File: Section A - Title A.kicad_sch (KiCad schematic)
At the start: 9 parts, among them J2 THD-02-R, J3 Conn_01x22_Female, J4 690-019-298-412, U2 RT9742SNGV

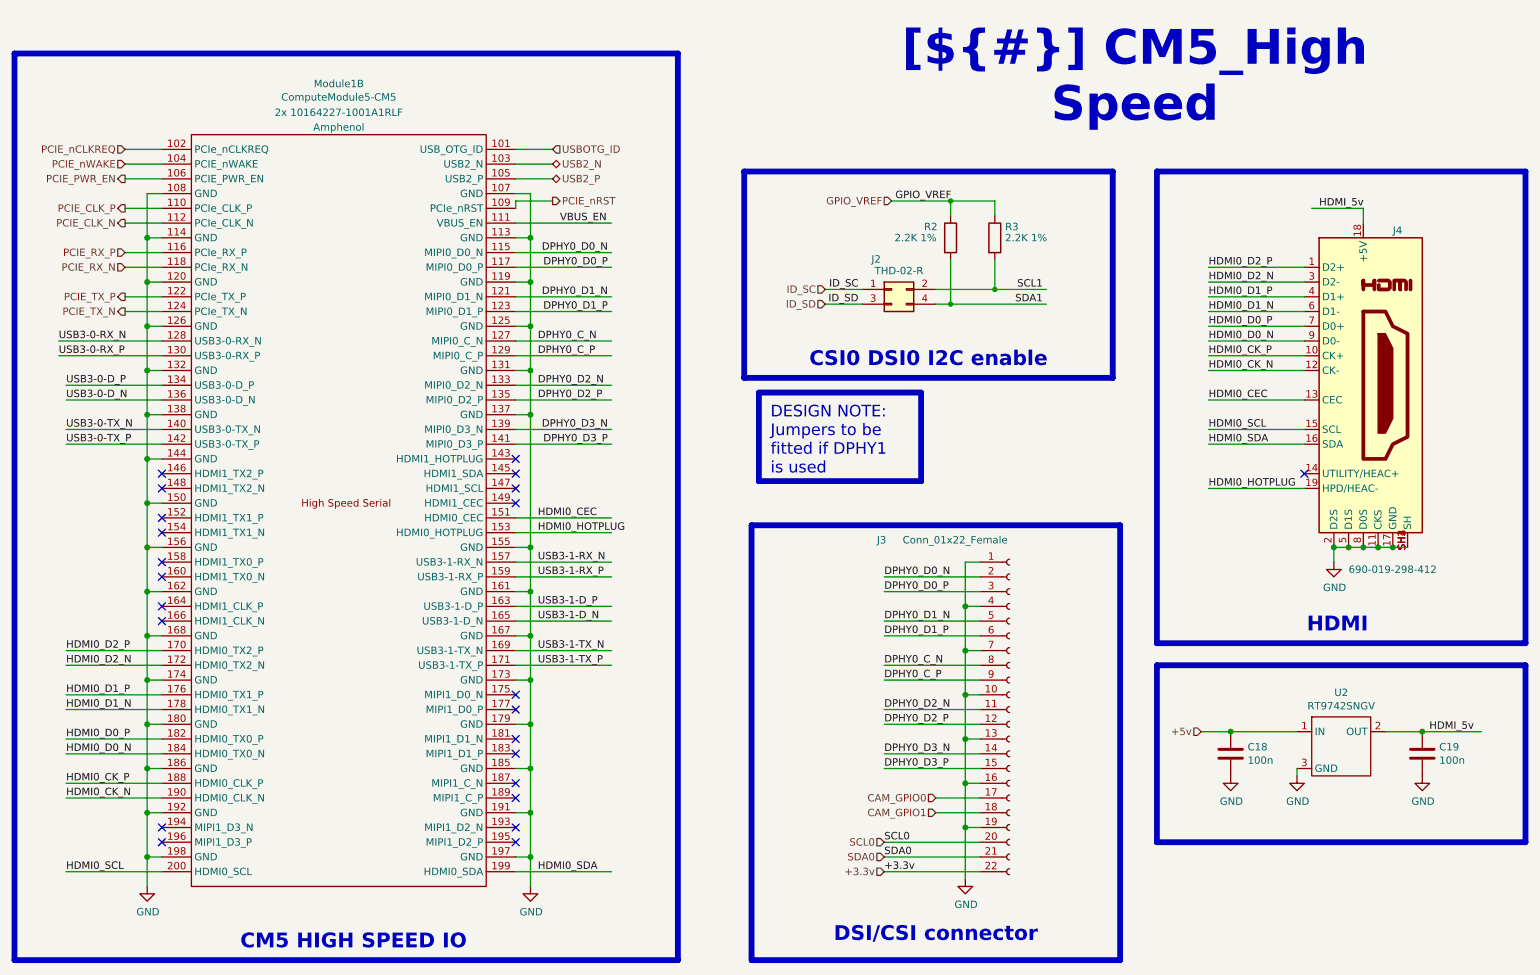
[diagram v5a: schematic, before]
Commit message: Swiitched to JSM561
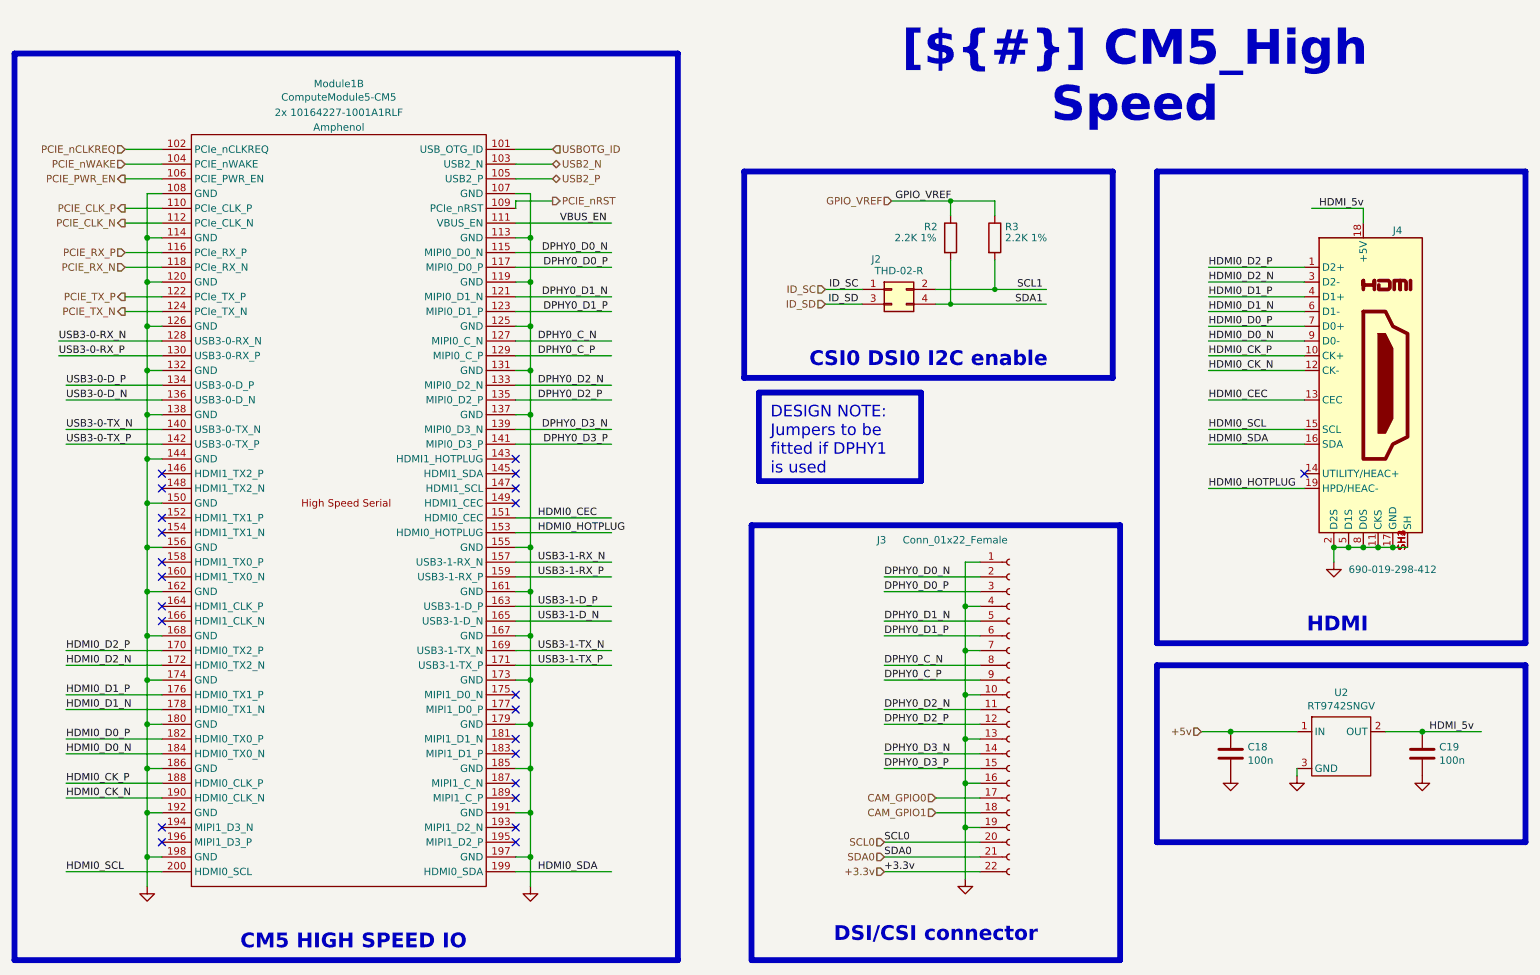
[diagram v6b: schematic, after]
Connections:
- removed net GND: C18.2, C19.2, J3.1 (Pin_1), J3.10 (Pin_10), J3.13 (Pin_13), J3.16 (Pin_16), J3.19 (Pin_19), J3.4 (Pin_4), J3.7 (Pin_7), J4.11 (CKS), J4.17 (GND), J4.2 (D2S), J4.5 (D1S), J4.8 (D0S), J4.SH1 (SH), J4.SH2 (SH), J4.SH3 (SH), J4.SH4 (SH), Module1.107 (GND), Module1.108 (GND), Module1.113 (GND), Module1.114 (GND), Module1.119 (GND), Module1.120 (GND), Module1.125 (GND), Module1.126 (GND), Module1.131 (GND), Module1.132 (GND), Module1.137 (GND), Module1.138 (GND), Module1.144 (GND), Module1.150 (GND), Module1.155 (GND), Module1.156 (GND), Module1.161 (GND), Module1.162 (GND), Module1.167 (GND), Module1.168 (GND), Module1.173 (GND), Module1.174 (GND), Module1.179 (GND), Module1.180 (GND), Module1.185 (GND), Module1.186 (GND), Module1.191 (GND), Module1.192 (GND), Module1.197 (GND), Module1.198 (GND), U2.3 (GND)
- new net: J3.1 (Pin_1), J3.10 (Pin_10), J3.13 (Pin_13), J3.16 (Pin_16), J3.19 (Pin_19), J3.4 (Pin_4), J3.7 (Pin_7)
- new net: J4.11 (CKS), J4.17 (GND), J4.2 (D2S), J4.5 (D1S), J4.8 (D0S), J4.SH1 (SH), J4.SH2 (SH), J4.SH3 (SH), J4.SH4 (SH)
- new net: Module1.107 (GND), Module1.113 (GND), Module1.119 (GND), Module1.125 (GND), Module1.131 (GND), Module1.137 (GND), Module1.155 (GND), Module1.161 (GND), Module1.167 (GND), Module1.173 (GND), Module1.179 (GND), Module1.185 (GND), Module1.191 (GND), Module1.197 (GND)
- new net: Module1.108 (GND), Module1.114 (GND), Module1.120 (GND), Module1.126 (GND), Module1.132 (GND), Module1.138 (GND), Module1.144 (GND), Module1.150 (GND), Module1.156 (GND), Module1.162 (GND), Module1.168 (GND), Module1.174 (GND), Module1.180 (GND), Module1.186 (GND), Module1.192 (GND), Module1.198 (GND)
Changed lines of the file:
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@@
 			)
 		)
-		(property "Value" "GND"
+		(property "Value" "~"
 			(at 242.697 108.5342 0)
 			(effects
@@
 			)
 		)
-		(property "Value" "GND"
+		(property "Value" "~"
 			(at 104.267 164.4142 0)
 			(effects
@@
 			)
 		)
-		(property "Value" "GND"
+		(property "Value" "~"
 			(at 38.227 164.4142 0)
 			(effects
@@
 			)
 		)
-		(property "Value" "GND"
+		(property "Value" "~"
 			(at 179.197 163.1442 0)
 			(effects
@@
 			)
 		)
-		(property "Value" "GND"
+		(property "Value" "~"
 			(at 257.937 145.3642 0)
 			(effects
@@
 			)
 		)
-		(property "Value" "GND"
+		(property "Value" "~"
 			(at 224.917 145.3642 0)
 			(effects
@@
 			)
 		)
-		(property "Value" "GND"
+		(property "Value" "~"
 			(at 236.347 145.3642 0)
 			(effects

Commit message: Removed Ethernet
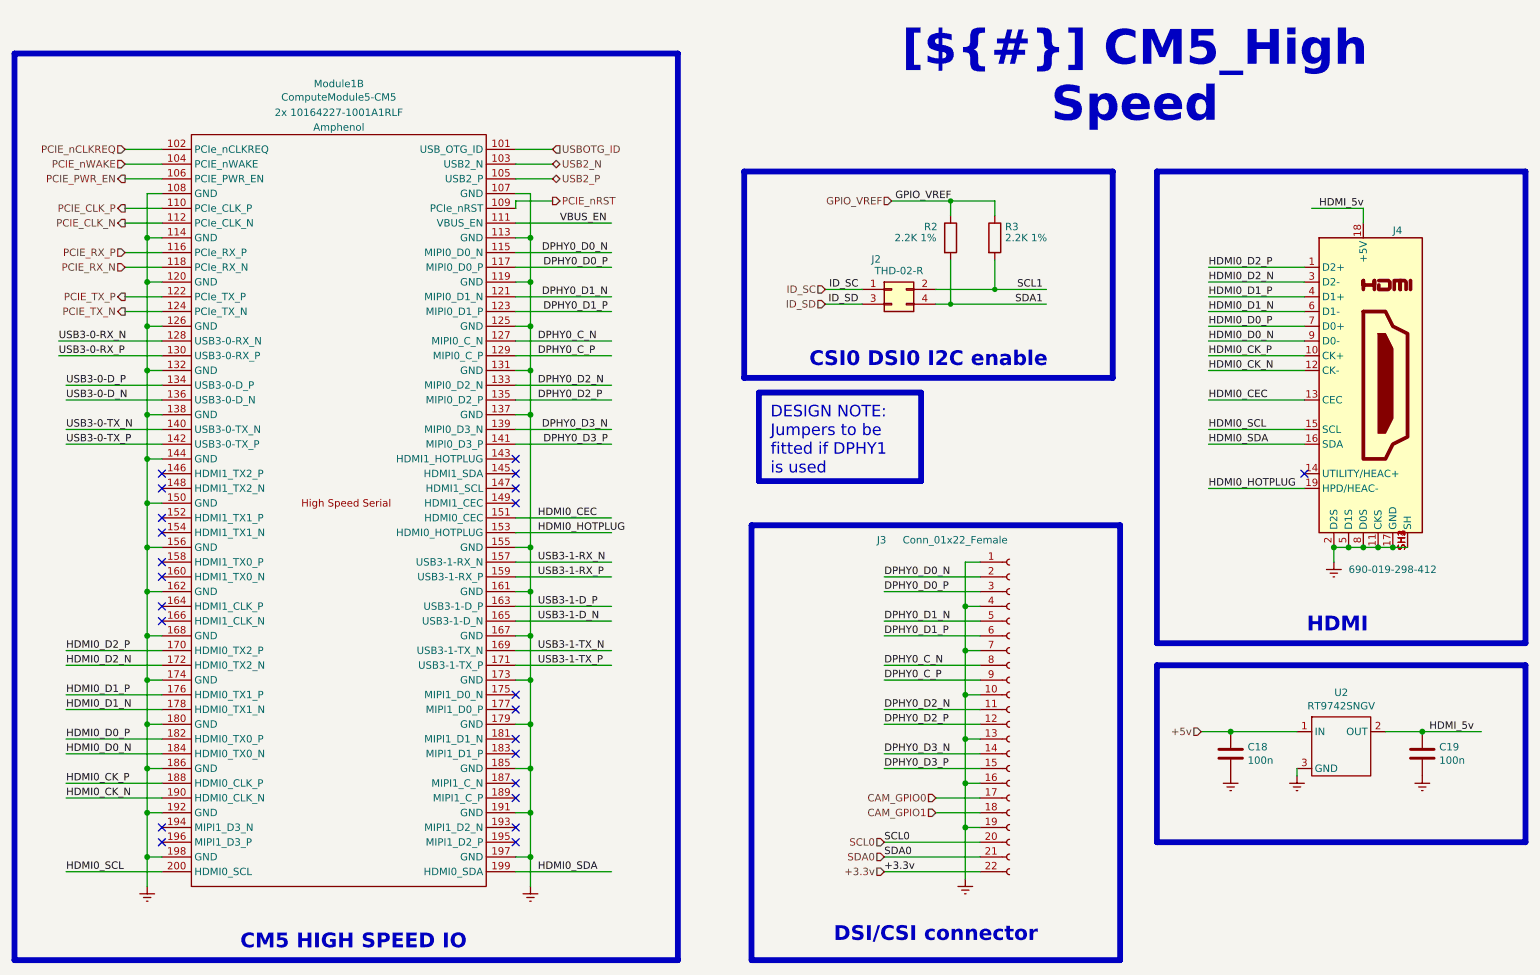
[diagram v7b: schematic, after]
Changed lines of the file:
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@@
 	)
 	(symbol
-		(lib_id "power:GND")
+		(lib_id "power:Earth")
 		(at 242.57 104.14 0)
 		(unit 1)
@@
 			)
 		)
-		(property "Datasheet" ""
+		(property "Datasheet" "~"
 			(at 242.57 104.14 0)
 			(effects
@@
 			)
 		)
-		(property "Description" "Power symbol creates a global label with name \"GND\" , ground"
+		(property "Description" "Power symbol creates a global label with name \"Earth\""
 			(at 242.57 104.14 0)
 			(effects
@@
 	)
 	(symbol
-		(lib_id "power:GND")
+		(lib_id "power:Earth")
 		(at 104.14 160.02 0)
 		(unit 1)
@@
 			)
 		)
-		(property "Datasheet" ""
+		(property "Datasheet" "~"
 			(at 104.14 160.02 0)
 			(effects
@@
 			)
 		)
-		(property "Description" "Power symbol creates a global label with name \"GND\" , ground"
+		(property "Description" "Power symbol creates a global label with name \"Earth\""
 			(at 104.14 160.02 0)
 			(effects
@@
 	)
 	(symbol
-		(lib_id "power:GND")
+		(lib_id "power:Earth")
 		(at 38.1 160.02 0)
 		(unit 1)
@@
 			)
 		)
-		(property "Datasheet" ""
+		(property "Datasheet" "~"
 			(at 38.1 160.02 0)
 			(effects
@@
 			)
 		)
-		(property "Description" "Power symbol creates a global label with name \"GND\" , ground"
+		(property "Description" "Power symbol creates a global label with name \"Earth\""
 			(at 38.1 160.02 0)
 			(effects
@@
 	)
 	(symbol
-		(lib_id "power:GND")
+		(lib_id "power:Earth")
 		(at 179.07 158.75 0)
 		(unit 1)
@@
 			)
 		)
-		(property "Datasheet" ""
+		(property "Datasheet" "~"
 			(at 179.07 158.75 0)
 			(effects
@@
 			)
 		)
-		(property "Description" "Power symbol creates a global label with name \"GND\" , ground"
+		(property "Description" "Power symbol creates a global label with name \"Earth\""
 			(at 179.07 158.75 0)
 			(effects
@@
 	)
 	(symbol
-		(lib_id "power:GND")
+		(lib_id "power:Earth")
 		(at 257.81 140.97 0)
 		(unit 1)
@@
 			)
 		)
-		(property "Datasheet" ""
+		(property "Datasheet" "~"
 			(at 257.81 140.97 0)
 			(effects
@@
 			)
 		)
-		(property "Description" "Power symbol creates a global label with name \"GND\" , ground"
+		(property "Description" "Power symbol creates a global label with name \"Earth\""
 			(at 257.81 140.97 0)
 			(effects
@@
 	)
 	(symbol
-		(lib_id "power:GND")
+		(lib_id "power:Earth")
 		(at 224.79 140.97 0)
 		(unit 1)
@@
 			)
 		)
-		(property "Datasheet" ""
+		(property "Datasheet" "~"
 			(at 224.79 140.97 0)
 			(effects
@@
 			)
 		)
-		(property "Description" "Power symbol creates a global label with name \"GND\" , ground"
+		(property "Description" "Power symbol creates a global label with name \"Earth\""
 			(at 224.79 140.97 0)
 			(effects
@@
 	)
 	(symbol
-		(lib_id "power:GND")
+		(lib_id "power:Earth")
 		(at 236.22 140.97 0)
 		(unit 1)
@@
 			)
 		)
-		(property "Datasheet" ""
+		(property "Datasheet" "~"
 			(at 236.22 140.97 0)
 			(effects
@@
 			)
 		)
-		(property "Description" "Power symbol creates a global label with name \"GND\" , ground"
+		(property "Description" "Power symbol creates a global label with name \"Earth\""
 			(at 236.22 140.97 0)
 			(effects

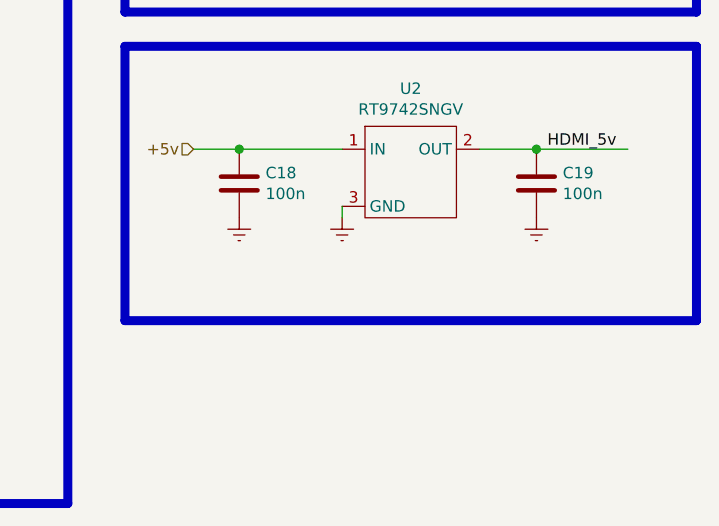
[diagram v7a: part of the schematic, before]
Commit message: Sheets neatened
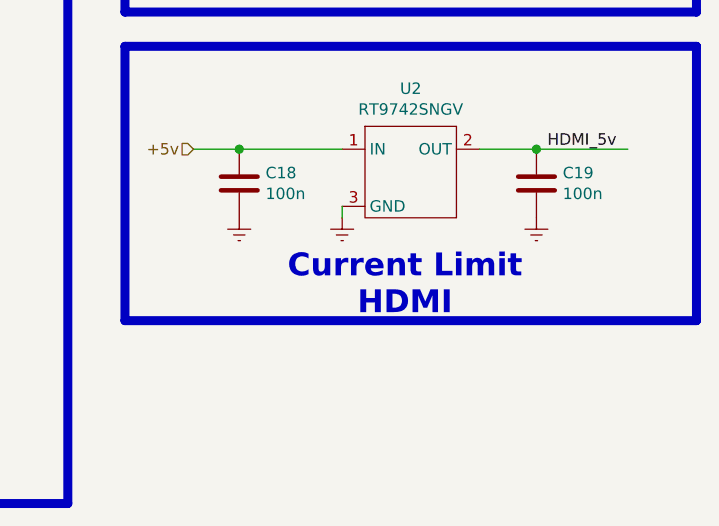
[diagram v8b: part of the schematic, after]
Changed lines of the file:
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@@
+		)
+	)
+	(text_box "Current Limit HDMI"
+		(exclude_from_sim no)
+		(at 228.6 146.05 0)
+		(size 29.21 7.62)
+		(margins 1.9049 1.9049 1.9049 1.9049)
+		(stroke
+			(width -0.0001)
+			(type solid)
+		)
+		(fill
+			(type none)
+		)
+		(effects
+			(font
+				(face "Times New Roman")
+				(size 2.54 2.54)
+				(thickness 0.508)
+				(bold yes)
+				(color 162 22 34 1)
+			)
+			(justify bottom)
 		)
 	)
